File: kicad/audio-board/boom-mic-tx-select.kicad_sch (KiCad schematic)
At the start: 14 parts, among them J4 BOOM_MIC_FROM_EARCUP, J5 TRS_TO_PJ068_AIRCRAFT, K1 G6K-2F-Y, Q1 2N7002, U11 ADP7118AUJZ-1.8-R7

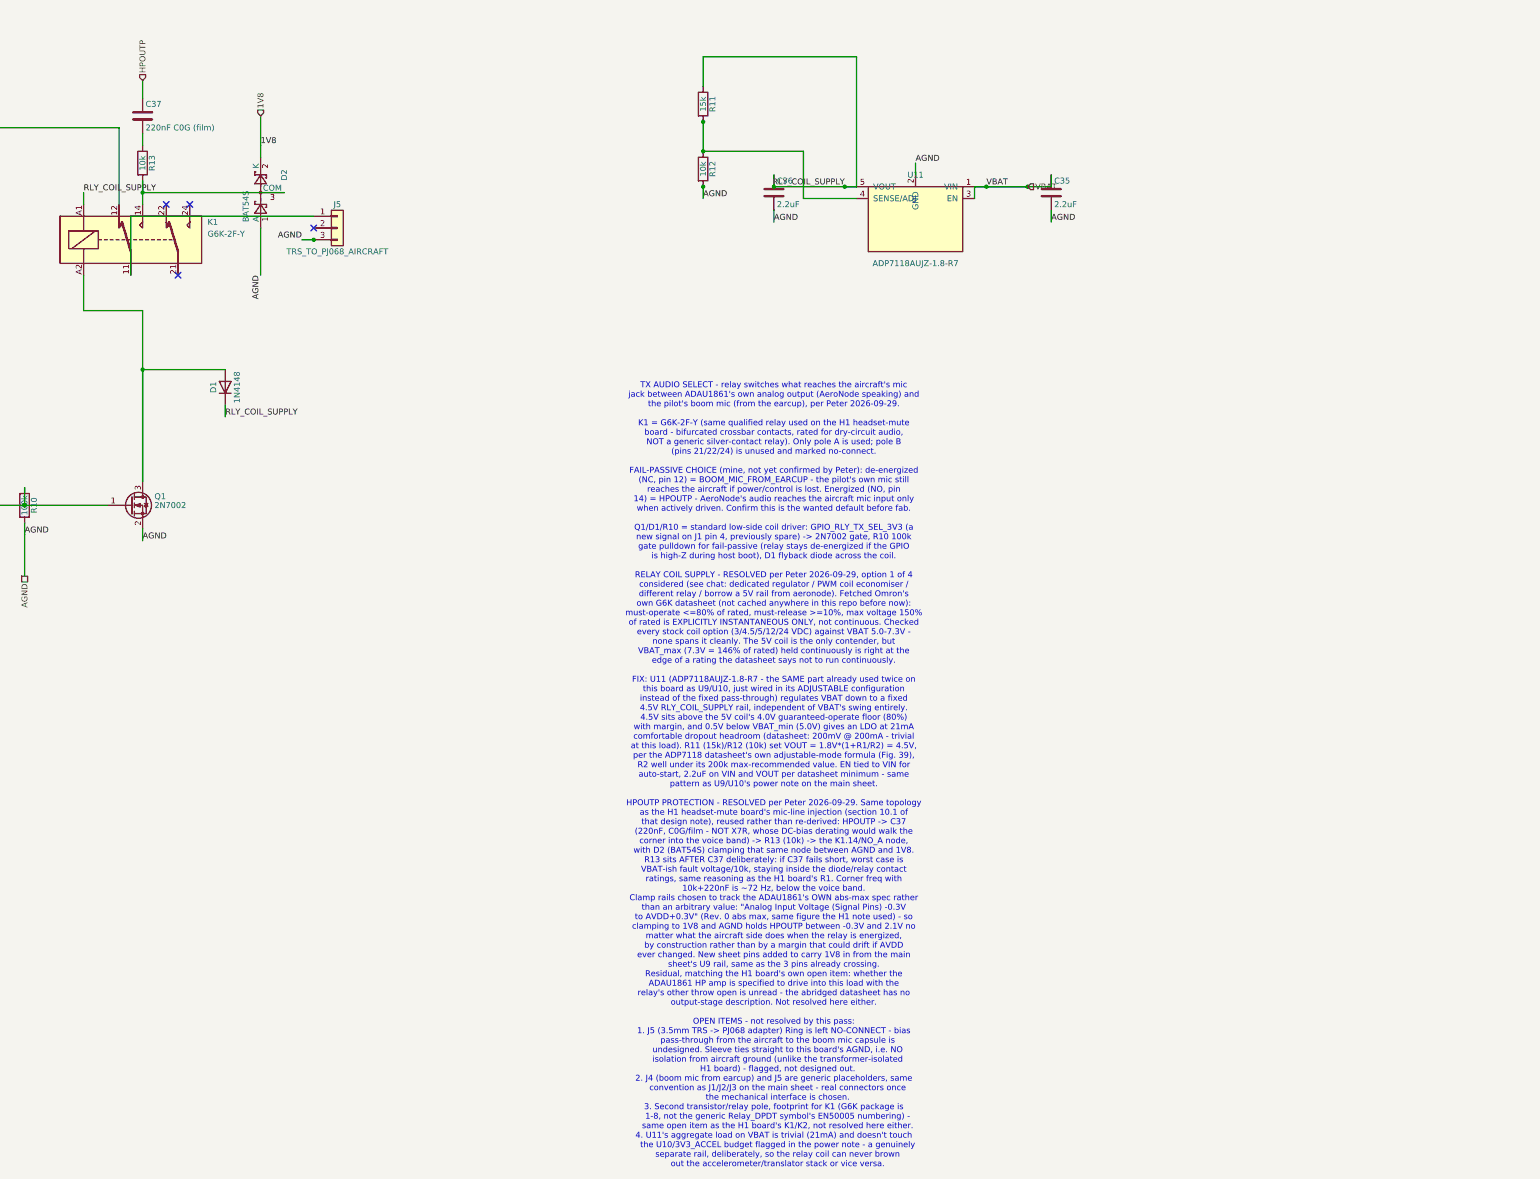
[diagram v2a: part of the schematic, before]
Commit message: [LIMA] add T1 (SM-LP-5001) for aircraft-side isolation, per Peter - replaces the C37/R13/D2-only network
Resolves the TRS ring/sleeve isolation question, and corrects a
mistake from two commits ago: the C37/R13/D2 network added for
HPOUTP protection cited the H1 headset-mute board's section 10.1,
but 10.1 was already superseded on that same board by its own
section 11 ("use the transformer approach for the aircraft side"),
which survives there only as a bench expedient. Missed that the
first time; caught reading the full H1 note before touching this
again.

Presented the tradeoff (H1's own §24-26 found the original ground-
loop argument for a transformer dead once AeroNode floats on
battery in flight, but a transformer's isolation is unconditional
where a cap+R+clamp's protection is calculated) and Peter ruled the
transformer for this board too, matching what H1 kept.

Per H1's section 11.2 circuit exactly:
- T1 (Bourns SM-LP-5001, 600:600 1:1, same part H1 uses) now sits
  between the relay and the TRS jack. HPOUTP/HPOUTN drive its
  primary directly and DIFFERENTIALLY through K1's two poles (both
  poles now used, not just pole A) - no DC to block, so C37 is
  gone entirely, and the "is the HP amp specified to run one leg
  unloaded" question closes because it no longer arises.
- R13 moved from the primary to the secondary (net MIC_LINE),
  per H1's explicit rule: an attenuator on the primary drags the
  LF corner into the voice band (419Hz for 10k into the 3.8H
  primary); on the secondary it sees only ~115R winding DCR (~5Hz).
- The secondary's other leg is a new net, AC_GND - the aircraft mic
  ground (J5 Sleeve) - explicitly separate from this board's AGND.
  Sleeve no longer bonds to AeroNode ground anywhere on this sheet.
- D2 (BAT54S) kept as belt-and-braces insurance per H1's own framing,
  now clamping HPOUTP directly rather than a node downstream of the
  removed C37/R13.

Generic Device:Transformer_1P_1S symbol used for T1, same as H1 -
its own note alr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
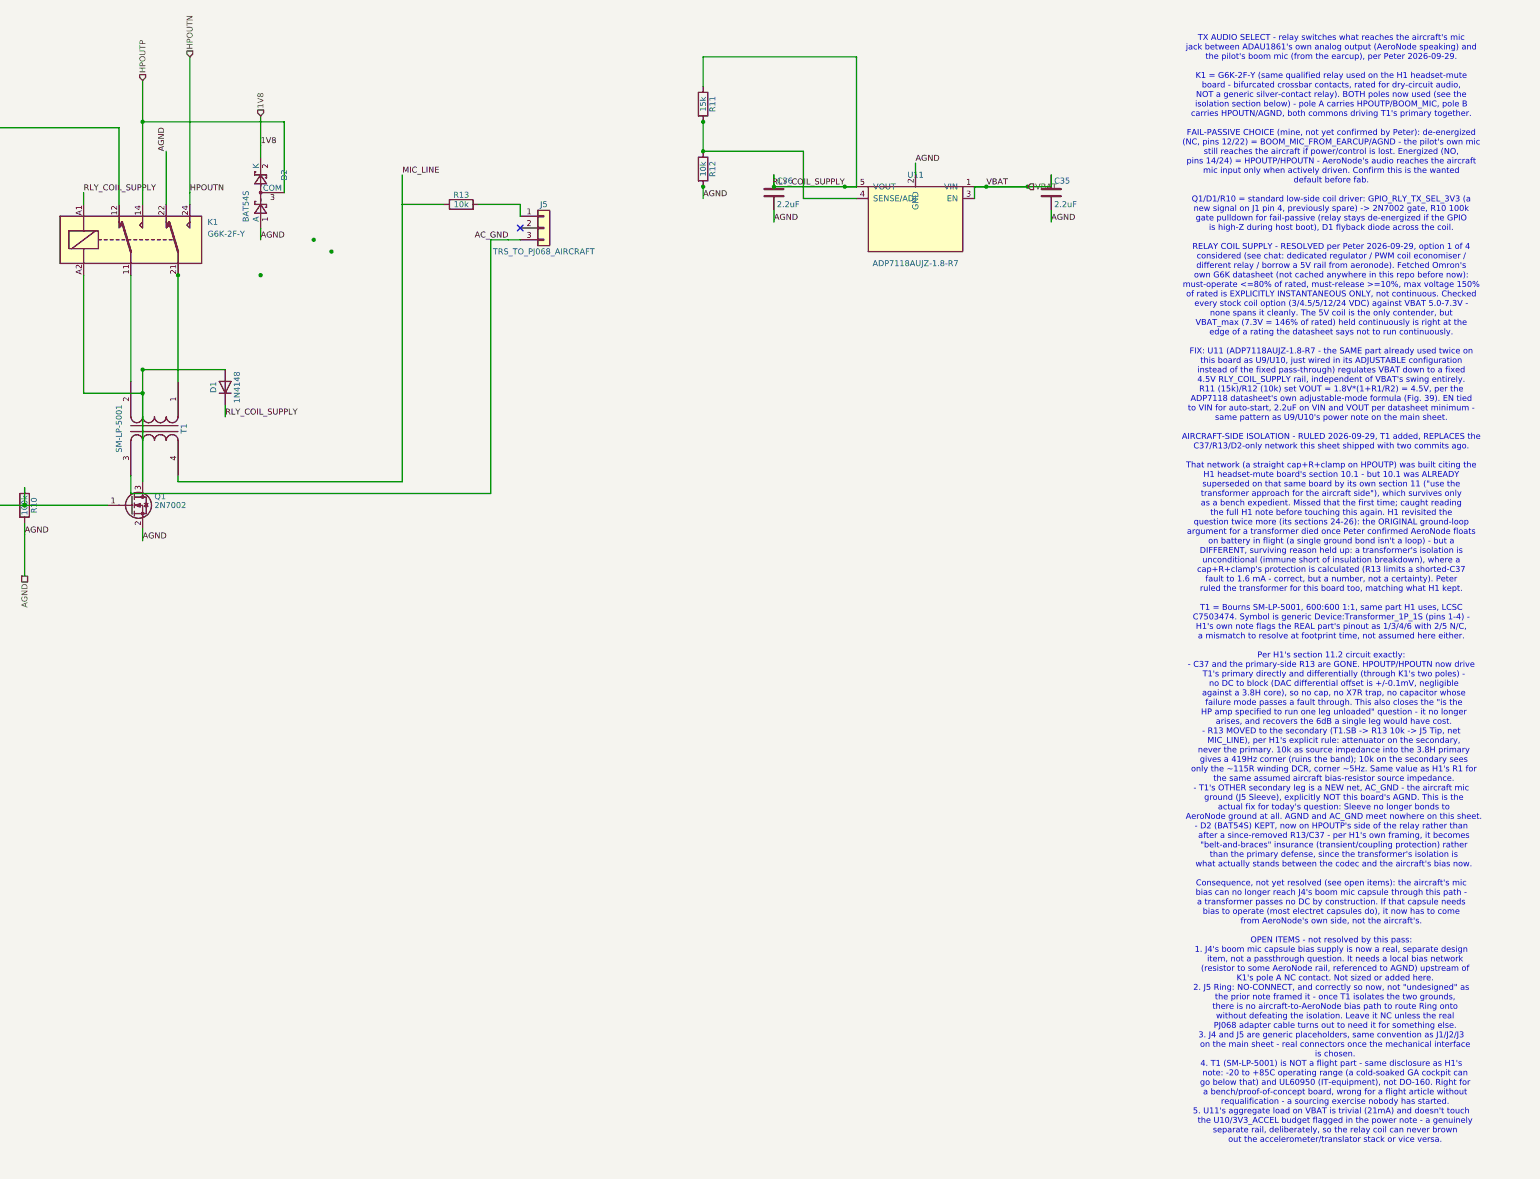
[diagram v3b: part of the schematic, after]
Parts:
- removed C37: 220nF C0G (film), symbol Device:C
- added T1: SM-LP-5001, symbol Device:Transformer_1P_1S
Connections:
- net AGND: now also K1.22; no longer J5.3 (Pin_3)
- net HPOUTP: now also D2.3 (COM), K1.14
- net MIC_LINE: now reaches R13.1
- net MIC_LINE: now also T1.4 (SB)
- net at K1.11: now also T1.2 (AB); no longer J5.1 (Pin_1)
- net at K1.21: now also T1.1 (AA)
- net HPOUTN: now reaches K1.24
- new net: J5.1 (Pin_1), R13.2
- new net AC_GND: J5.3 (Pin_3), T1.3 (SA)
- no-connect marks 4 -> 1
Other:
- note added: "TX AUDIO SELECT - relay switches what reaches the aircraft's mic jack between ADAU1861's own analog output (AeroNode speaking) and the pilot's boom mic (from the earcup), per Peter 2026-09-29. K1 = G6K-2F-Y (same qualified relay used on the H1 headset-mute board - bifurcated crossbar contacts, rated for dry-circuit audio, NOT a generic silver-contact relay). BOTH poles now used (see the isolation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"
- note removed: "TX AUDIO SELECT - relay switches what reaches the aircraft's mic jack between ADAU1861's own analog output (AeroNode speaking) and the pilot's boom mic (from the earcup), per Peter 2026-09-29. K1 = G6K-2F-Y (same qualified relay used on the H1 headset-mute board - bifurcated crossbar contacts, rated for dry-circuit audio, NOT a generic silver-contact relay). Only pole A is used; pole B (pins 21/2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"
- moved on the sheet: J5

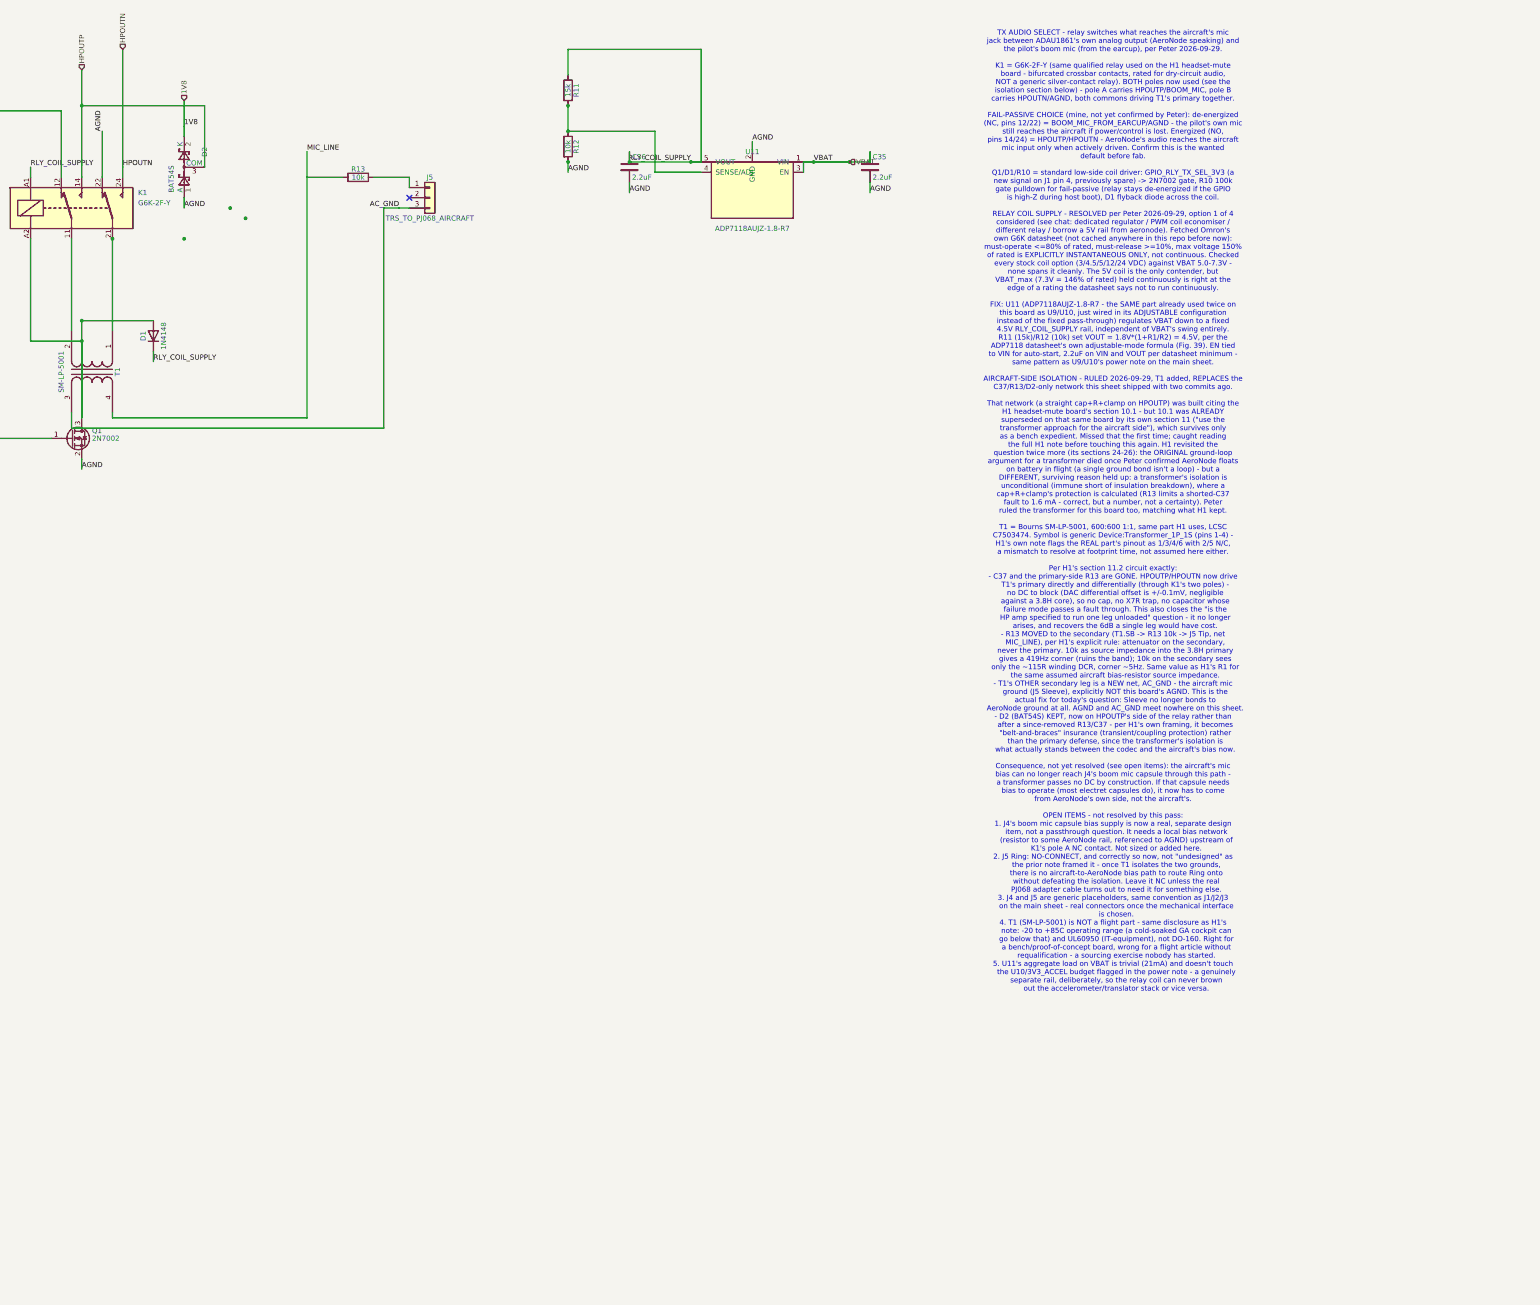
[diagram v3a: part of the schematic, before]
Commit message: [LIMA] revert to single-ended HPOUTP + blocking cap, resize R13 to match the real mic, per Peter
Two changes from Peter, implemented together.

1. Single-ended drive, not differential. HPOUTN backed out (sheet
pin, hierarchical label, U1 wiring all reverted to no-connect); K1
pole B unused again. T1's primary is now HPOUTP (via K1 pole A) on
one leg, AGND fixed on the other. This needed a new capacitor, C38
(2.2uF) in series with HPOUTP - not for the old reason (blocking the
aircraft's 8-16V mic bias, which T1 already handles unconditionally)
but a different one: HPOUTP sits at the DAC's ~0.85V common-mode
bias, and grounding the primary's other leg directly would push
that DC across the winding continuously (~7.4mA toward core
saturation) without a cap in the way.

Checked the ADAU186x Hardware Reference Manual (UG-2257, cached in
this repo) on whether single-ended output is actually documented:
it isn't. The output stage is described as differential throughout,
and unlike the analog inputs (explicit single-ended mode + an
AINx_INPUT_MODE register bit), there is no equivalent output mode
in prose or in the HP_CTRL register. Recorded as a flagged residual,
not resolved by adding the cap - the cap fixes the DC problem, it
doesn't make this a specified configuration.

Also recorded a firmware-adjacent finding from the same manual:
HP_MODE (HP_CTRL bit 0) should be set to line-out (1), not the
headphone-mode (0) reset default - T1's primary presents 7-72k of
inductive reactance across the voice band, a line-out load, not a
headphone one (rated >=10 ohm) load.

2. R13 resized 10k -> 470R. It had been copied from the H1 board's
R1 without checking it against this mic. The already-fetched Bose
A20 reference (docs/h1-headset-mute-relay.md) gives the mic's own
source impedance as 220-2200 ohm (the bias resistor) - our path at
10k presented 20-40x that, and delivered only 35mV rms against the
mic's 600mV/114dB SPL rating. At 470R the presented impedance
(585R with T1's windi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
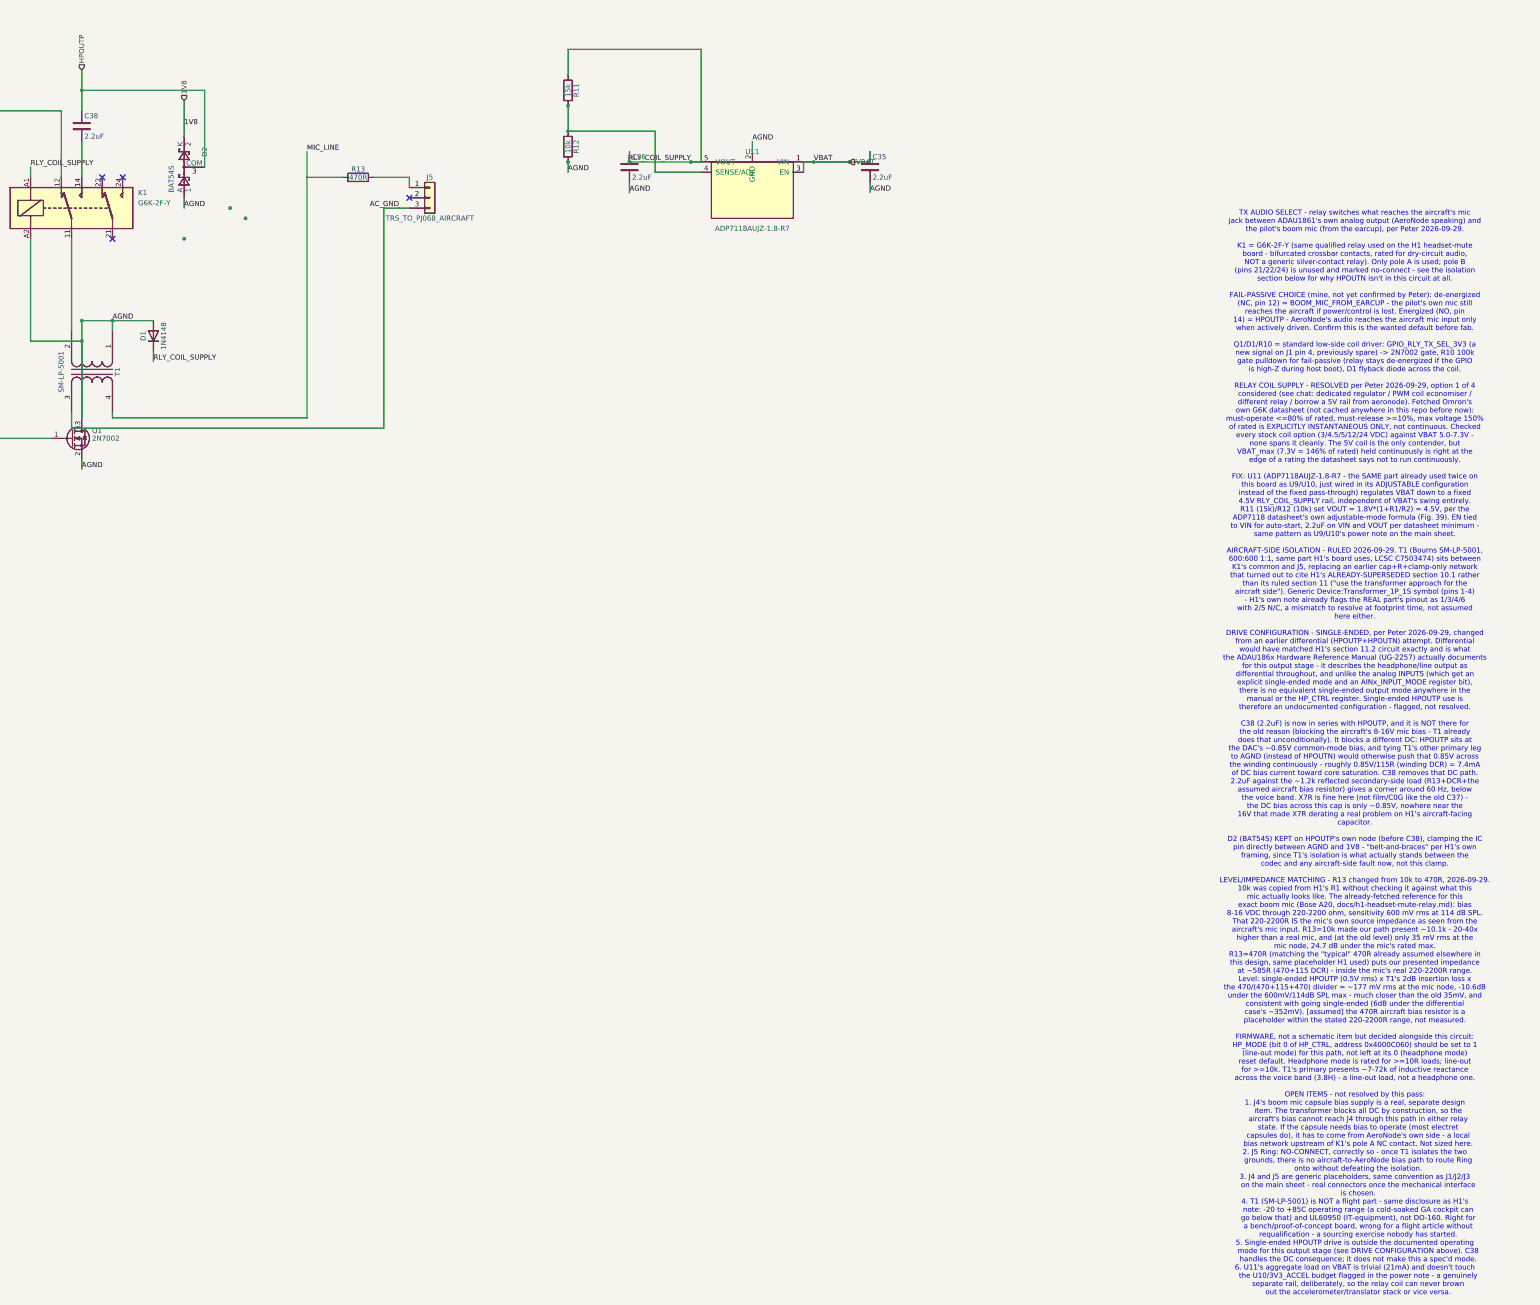
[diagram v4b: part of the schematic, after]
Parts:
- added C38: 2.2uF, symbol Device:C
- R13: value 10k -> 470R
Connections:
- net AGND: now also D1.2 (A), K1.A2, Q1.3 (D), T1.1 (AA); no longer K1.22
- net HPOUTP: now also C38.1; no longer K1.14
- net at K1.21: no longer T1.1 (AA)
- net HPOUTN: no longer names the net of K1.24
- new net: C38.2, K1.14
- no-connect marks 1 -> 4
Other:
- note added: "TX AUDIO SELECT - relay switches what reaches the aircraft's mic jack between ADAU1861's own analog output (AeroNode speaking) and the pilot's boom mic (from the earcup), per Peter 2026-09-29. K1 = G6K-2F-Y (same qualified relay used on the H1 headset-mute board - bifurcated crossbar contacts, rated for dry-circuit audio, NOT a generic silver-contact relay). Only pole A is used; pole B (pins 21/2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"
- note removed: "TX AUDIO SELECT - relay switches what reaches the aircraft's mic jack between ADAU1861's own analog output (AeroNode speaking) and the pilot's boom mic (from the earcup), per Peter 2026-09-29. K1 = G6K-2F-Y (same qualified relay used on the H1 headset-mute board - bifurcated crossbar contacts, rated for dry-circuit audio, NOT a generic silver-contact relay). BOTH poles now used (see the isolation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"
